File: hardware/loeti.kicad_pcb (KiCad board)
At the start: 4 copper layers, 80 x 50.5 mm, 94 parts, among them J1 REDFIT_SWD_6, J2 USB_C_Receptacle_USB2.0, J3 AudioJack3, Q1 BC817, Q2 FDS6630A, Q3 Si4425FDY, Q4 BC817, Q5 BC807, SW1 BOOT, SW2 RotaryEncoder_Switch, U1 USBLC6-2SC6, U2 EA_OLEDS102-6, U3 M24C64-RMN, U4 STM32G431CBTx, U5 AMS1117-3.3, U6 74AHC1G08, U7 Opamp_Dual, U9 INA301, X1 SG-210STF (16 MHz)

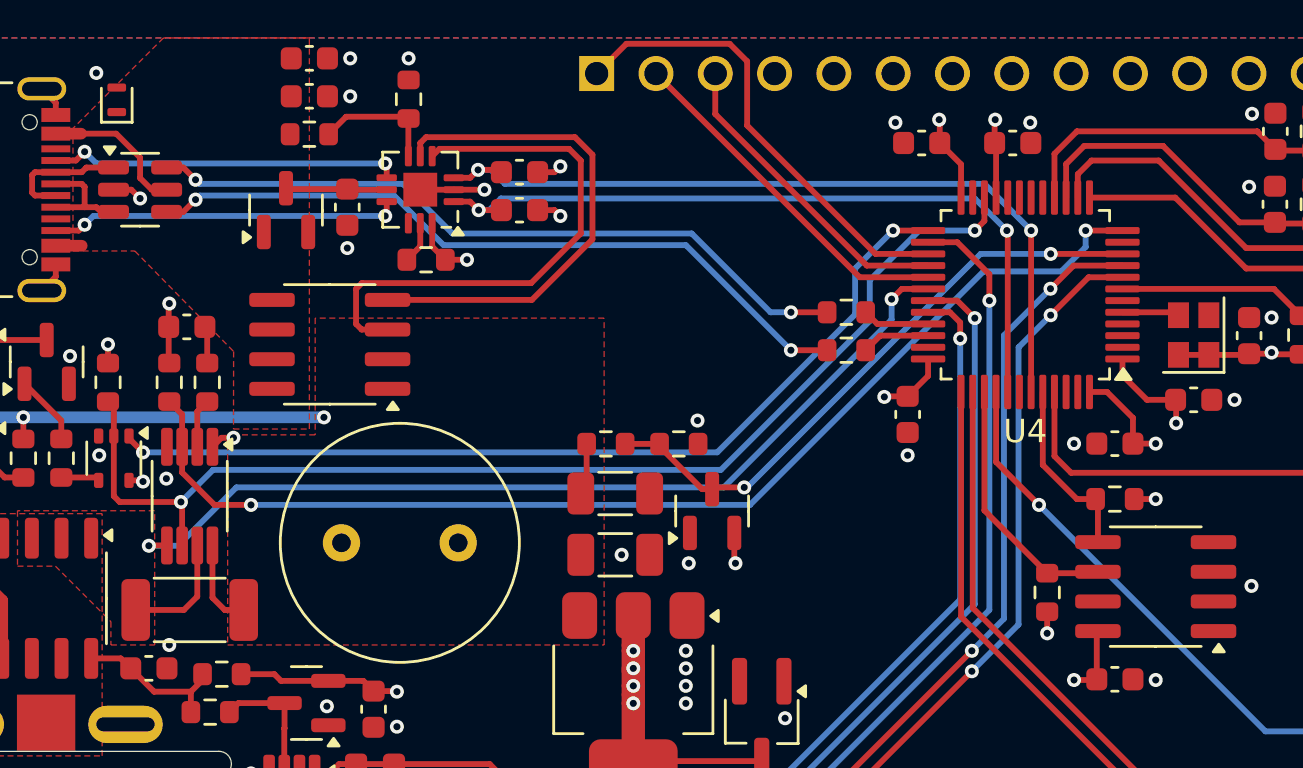
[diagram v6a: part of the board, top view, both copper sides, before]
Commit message: fix: adc assignments
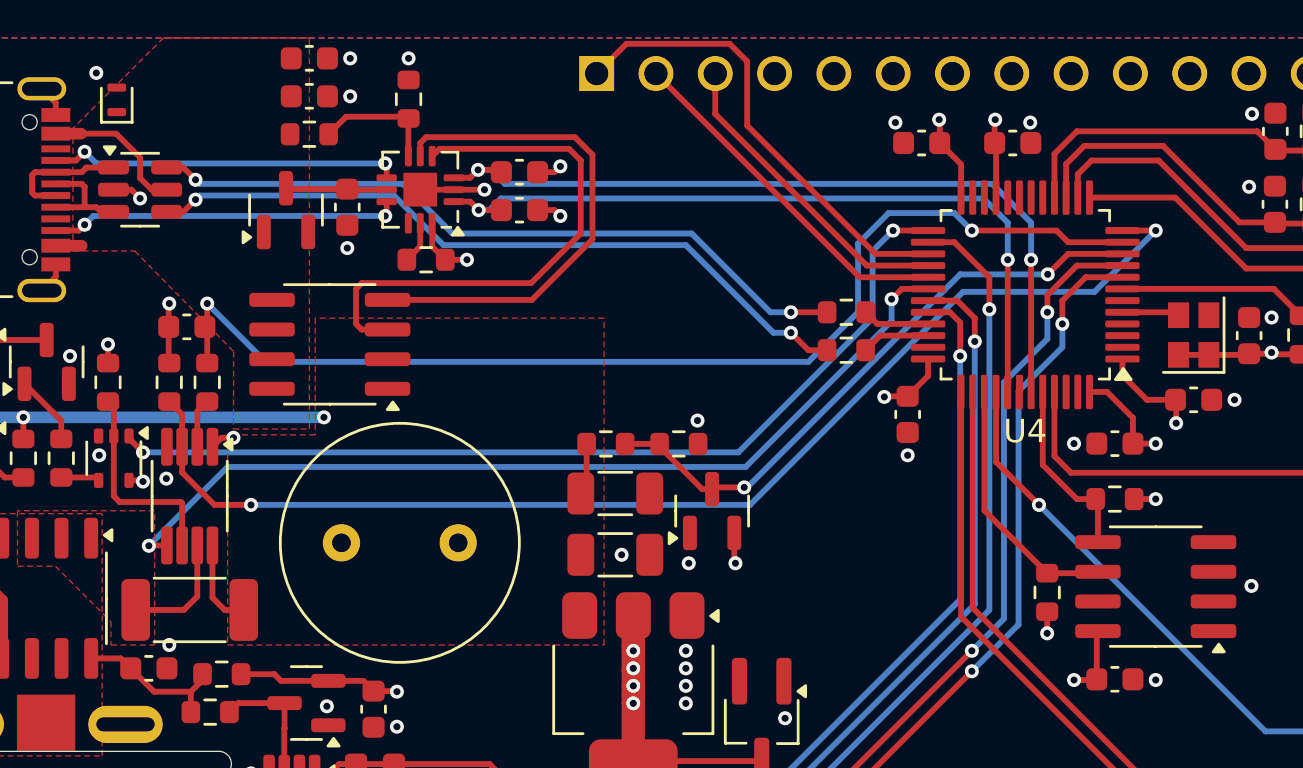
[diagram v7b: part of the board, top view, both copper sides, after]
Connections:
- net /ADC2_IN3 renamed /ADC1_IN3
- C32 pad 1: /CURR_OUT -> /ADC1_IN4
- R29 pad 1: /CURR_OUT -> /ADC1_IN4
- U4 pad 11: unconnected-(U4-PA3-Pad11) -> /ADC1_IN4
- U4 pad 22: /CURR_ALERT -> unconnected-(U4-PB10-Pad22)
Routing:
- net /ADC1_IN4: track 0.00 -> 47.6 mm, vias 0 -> 2
- net /CURR_ALERT: track 50.1 -> 8.66 mm, vias 2 -> 0
- net /DAC1_OUT1: track 49.4 -> 51.8 mm
- net /CURR_OUT: track 1.45 -> 0.00 mm
- net /TIM2_CH4: track 39.6 -> 40.1 mm

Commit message: feat: add further pins
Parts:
- moved C18 1.67 mm to (149.2, 82.2)
- moved C16 0.90 mm to (153.1, 80.2), turned to 90 degrees
- moved C13 0.40 mm to (124.8, 97.8)
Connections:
- U4 pad 14: /ROT_SW -> unconnected-(U4-PA6-Pad14)
- U4 pad 15: /ROT_A -> unconnected-(U4-PA7-Pad15)
- U4 pad 16: /ROT_B -> /ROT_SW
- U4 pad 17: unconnected-(U4-PB1-Pad17) -> /ROT_A
- U4 pad 18: unconnected-(U4-PB2-Pad18) -> /ROT_B
- U4 pad 4: unconnected-(U4-PC15-Pad4) -> /CURR_ALERT
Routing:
- net /CURR_ALERT: track 8.66 -> 52.6 mm, vias 0 -> 2
- net /ROT_SW: track 18.1 -> 19.2 mm
- net /ROT_A: track 13.7 -> 14.7 mm
- net /ROT_B: track 13.6 -> 14.6 mm
- net +3V3: track 72.4 -> 71.5 mm
